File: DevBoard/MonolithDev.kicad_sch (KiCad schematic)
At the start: 4 parts

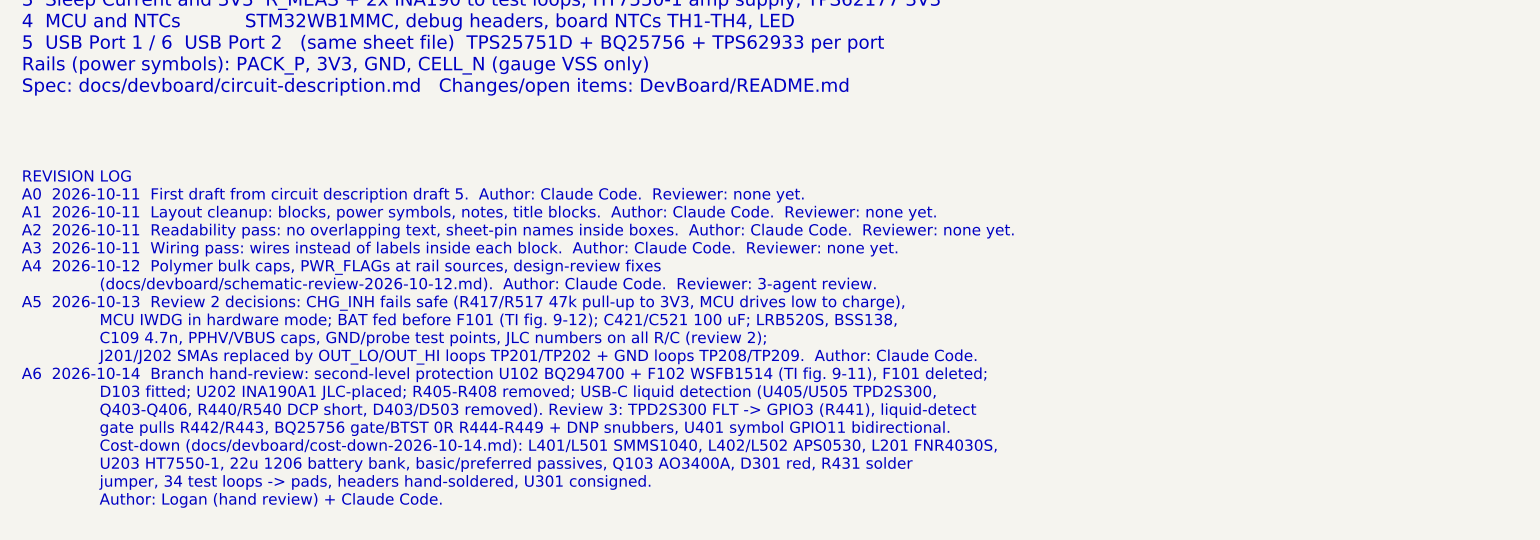
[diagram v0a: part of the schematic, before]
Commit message: Dev board: charger half-bridges -> discrete PGQ04N070 FETs
Each IAUC45N04S6L063H half-bridge ($1.16, 62 at JLC) becomes two JinYu
PGQ04N070 (C49384056, $0.12, PDFN3333 on the AGM PDFN3.3x3.3 footprint):
Q401/Q407 USB side, Q402/Q408 battery side, and the 5xx twins. 40 V,
10 mOhm max at 4.5 V (IAUC45: 8.5), Qg 14.7 nC; matches the production
plan of discrete 3.3 x 3.3 mm FETs. New PGQ04N070 symbol, power stage
redrawn, docs and costed BOM updated: about $77 per board at 5 boards.

Co-Authored-By: Claude Opus 5.5 <noreply@anthropic.com>
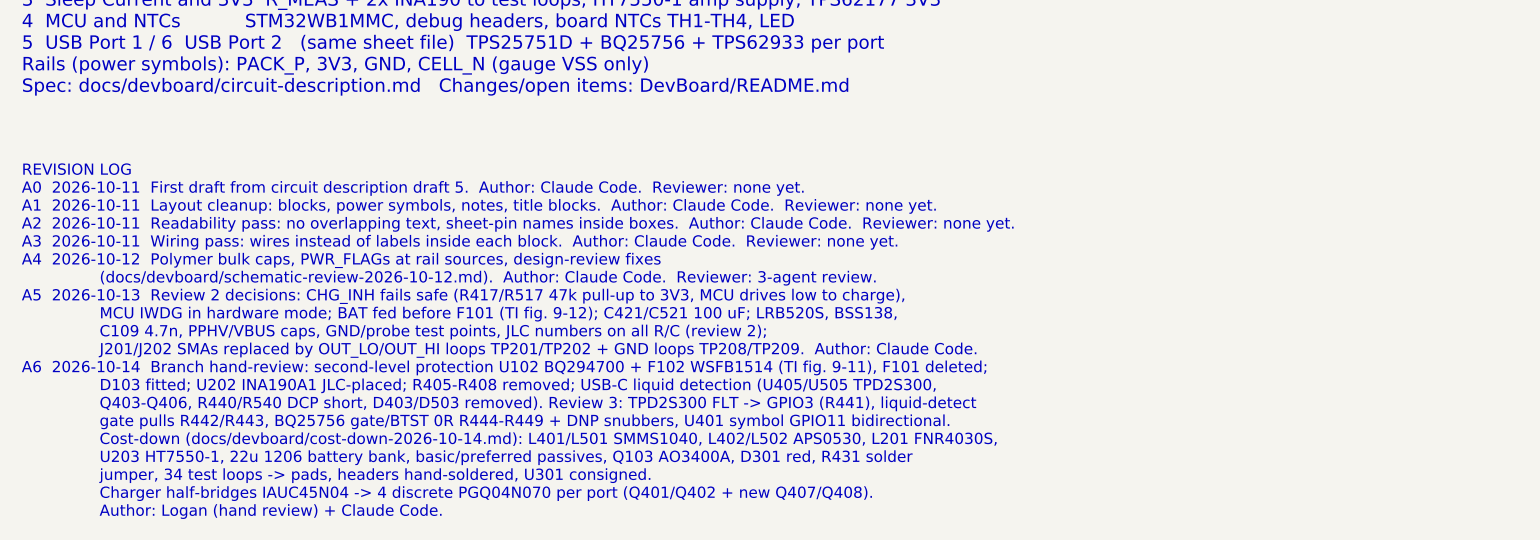
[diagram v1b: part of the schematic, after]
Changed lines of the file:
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@@
 		)
 	)
-	(text "REVISION LOG\nA0  2026-10-11  First draft from circuit description draft 5.  Author: Claude Code.  Reviewer: none yet.\nA1  2026-10-11  Layout cleanup: blocks, power symbols, notes, title blocks.  Author: Claude Code.  Reviewer: none yet.\nA2  2026-10-11  Readability pass: no overlapping text, sheet-pin names inside boxes.  Author: Claude Code.  Reviewer: none yet.\nA3  2026-10-11  Wiring pass: wires instead of labels inside each block.  Author: Claude Code.  Reviewer: none yet.\nA4  2026-10-12  Polymer bulk caps, PWR_FLAGs at rail sources, design-review fixes\n                (docs/devboard/schematic-review-2026-10-12.md).  Author: Claude Code.  Reviewer: 3-agent review.\nA5  2026-10-13  Review 2 decisions: CHG_INH fails safe (R417/R517 47k pull-up to 3V3, MCU drives low to charge),\n                MCU IWDG in hardware mode; BAT fed before F101 (TI fig. 9-12); C421/C521 100 uF; LRB520S, BSS138,\n                C109 4.7n, PPHV/VBUS caps, GND/probe test points, JLC numbers on all R/C (review 2);\n                J201/J202 SMAs replaced by OUT_LO/OUT_HI loops TP201/TP202 + GND loops TP208/TP209.  Author: Claude Code.\nA6  2026-10-14  Branch hand-review: second-level protection U102 BQ294700 + F102 WSFB1514 (TI fig. 9-11), F101 deleted;\n                D103 fitted; U202 INA190A1 JLC-placed; R405-R408 removed; USB-C liquid detection (U405/U505 TPD2S300,\n                Q403-Q406, R440/R540 DCP short, D403/D503 removed). Review 3: TPD2S300 FLT -> GPIO3 (R441), liquid-detect\n                gate pulls R442/R443, BQ25756 gate/BTST 0R R444-R449 + DNP snubbers, U401 symbol GPIO11 bidirectional.\n                Cost-down (docs/devboard/cost-down-2026-10-14.md): L401/L501 SMMS1040, L402/L502 APS0530, L201 FNR4030S,\n                U203 HT7550-1, 22u 1206 battery bank, basic/preferred passives, Q103 AO3400A, D301 red, R431 solder\n                jumper, 34 test loops -> pads, headers hand-soldered, U301 consigned.\n                Author: Logan (hand review) + Claude Code."
+	(text "REVISION LOG\nA0  2026-10-11  First draft from circuit description draft 5.  Author: Claude Code.  Reviewer: none yet.\nA1  2026-10-11  Layout cleanup: blocks, power symbols, notes, title blocks.  Author: Claude Code.  Reviewer: none yet.\nA2  2026-10-11  Readability pass: no overlapping text, sheet-pin names inside boxes.  Author: Claude Code.  Reviewer: none yet.\nA3  2026-10-11  Wiring pass: wires instead of labels inside each block.  Author: Claude Code.  Reviewer: none yet.\nA4  2026-10-12  Polymer bulk caps, PWR_FLAGs at rail sources, design-review fixes\n                (docs/devboard/schematic-review-2026-10-12.md).  Author: Claude Code.  Reviewer: 3-agent review.\nA5  2026-10-13  Review 2 decisions: CHG_INH fails safe (R417/R517 47k pull-up to 3V3, MCU drives low to charge),\n                MCU IWDG in hardware mode; BAT fed before F101 (TI fig. 9-12); C421/C521 100 uF; LRB520S, BSS138,\n                C109 4.7n, PPHV/VBUS caps, GND/probe test points, JLC numbers on all R/C (review 2);\n                J201/J202 SMAs replaced by OUT_LO/OUT_HI loops TP201/TP202 + GND loops TP208/TP209.  Author: Claude Code.\nA6  2026-10-14  Branch hand-review: second-level protection U102 BQ294700 + F102 WSFB1514 (TI fig. 9-11), F101 deleted;\n                D103 fitted; U202 INA190A1 JLC-placed; R405-R408 removed; USB-C liquid detection (U405/U505 TPD2S300,\n                Q403-Q406, R440/R540 DCP short, D403/D503 removed). Review 3: TPD2S300 FLT -> GPIO3 (R441), liquid-detect\n                gate pulls R442/R443, BQ25756 gate/BTST 0R R444-R449 + DNP snubbers, U401 symbol GPIO11 bidirectional.\n                Cost-down (docs/devboard/cost-down-2026-10-14.md): L401/L501 SMMS1040, L402/L502 APS0530, L201 FNR4030S,\n                U203 HT7550-1, 22u 1206 battery bank, basic/preferred passives, Q103 AO3400A, D301 red, R431 solder\n                jumper, 34 test loops -> pads, headers hand-soldered, U301 consigned.\n                Charger half-bridges IAUC45N04 -> 4 discrete PGQ04N070 per port (Q401/Q402 + new Q407/Q408).\n                Author: Logan (hand review) + Claude Code."
 		(exclude_from_sim no)
-		(at 30.48 252.73 0)
+		(at 30.48 254.0 0)
 		(effects
 			(font

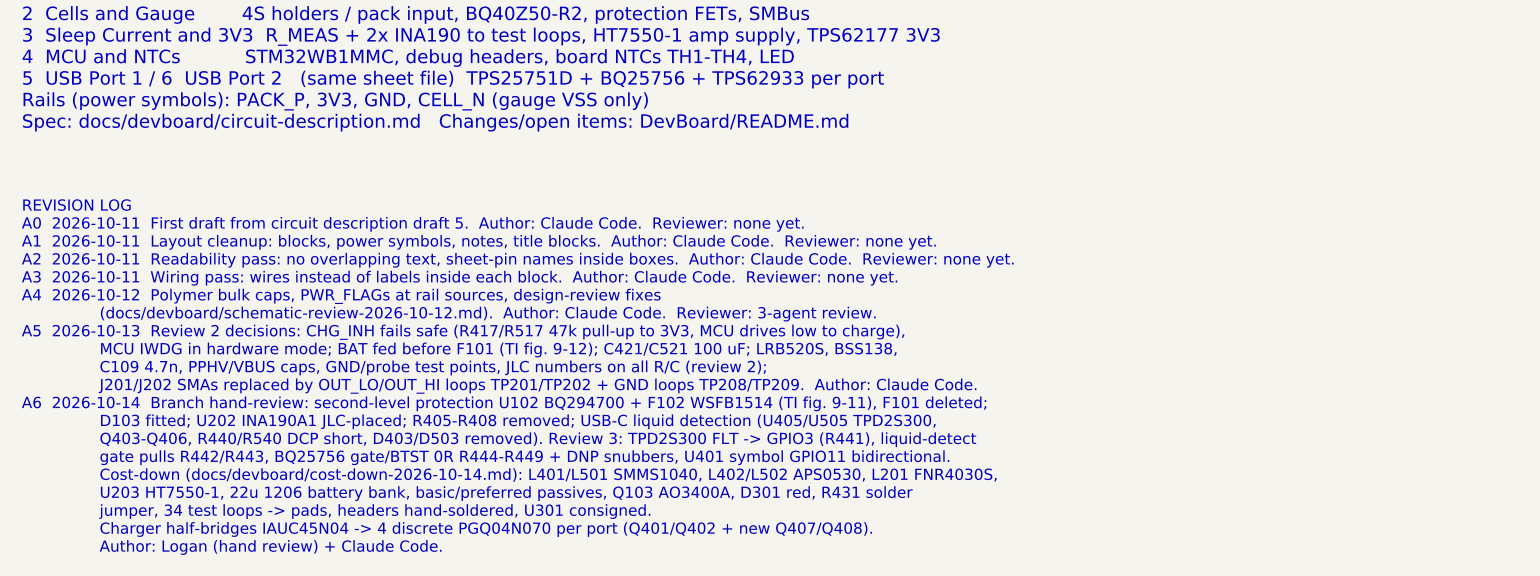
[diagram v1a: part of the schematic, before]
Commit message: Dev board: 6-layer 1.6 mm board, TPD4S201 port protector, 1.6 mm USB-C
- Stack-up: 6 layers, 1.6 mm, 2 oz outer / 0.5 oz inner (In1/In4 GND),
  0.3 mm drill / 0.45 mm via minimum so JLC's small-via surcharge is gone.
  Via-in-pad (POFV) is free on 6+ layers.
- U405/U505: TPD2S300 (0.4 mm DSBGA) -> TPD4S201TRGRRQ1 (VQFN-20 RGR),
  CC + SBU protection with FLT -> GPIO3. D402/D502 and C453/C553 removed.
- J401/J501: Shou Han TYPE-C 16PCB1.6 IP68 (C55629729), footprint and
  STEP model generated for the 1.6 mm board.
- TPS25751 REF0038A thermal vias 0.2 -> 0.3 mm.
- setup_board.py keeps unmanaged net classes (Kelvin); reset_board.py
  reloads swapped footprints in place.
- ERC 0 errors, DRC schematic parity 0. BOM $77.17 -> $78.65 per board
  at 5 boards.

Co-Authored-By: Claude Opus 5.5 <noreply@anthropic.com>
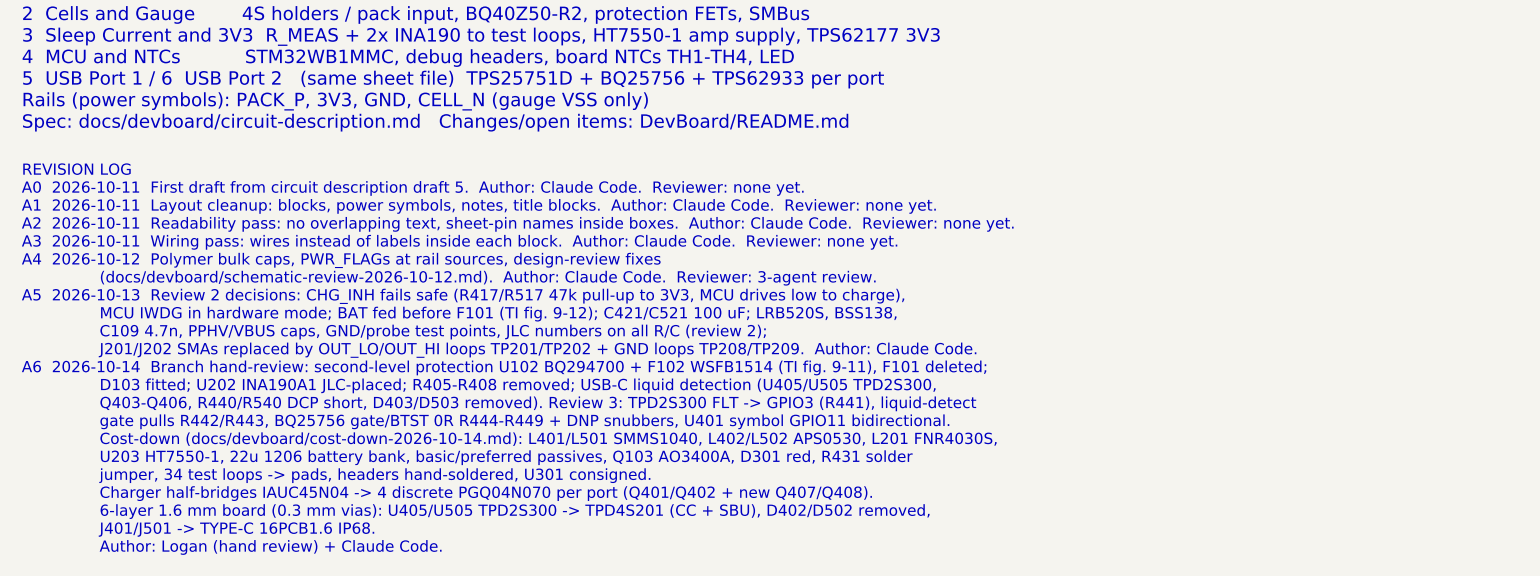
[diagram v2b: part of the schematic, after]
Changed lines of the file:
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@@
 		)
 	)
-	(text "REVISION LOG\nA0  2026-10-11  First draft from circuit description draft 5.  Author: Claude Code.  Reviewer: none yet.\nA1  2026-10-11  Layout cleanup: blocks, power symbols, notes, title blocks.  Author: Claude Code.  Reviewer: none yet.\nA2  2026-10-11  Readability pass: no overlapping text, sheet-pin names inside boxes.  Author: Claude Code.  Reviewer: none yet.\nA3  2026-10-11  Wiring pass: wires instead of labels inside each block.  Author: Claude Code.  Reviewer: none yet.\nA4  2026-10-12  Polymer bulk caps, PWR_FLAGs at rail sources, design-review fixes\n                (docs/devboard/schematic-review-2026-10-12.md).  Author: Claude Code.  Reviewer: 3-agent review.\nA5  2026-10-13  Review 2 decisions: CHG_INH fails safe (R417/R517 47k pull-up to 3V3, MCU drives low to charge),\n                MCU IWDG in hardware mode; BAT fed before F101 (TI fig. 9-12); C421/C521 100 uF; LRB520S, BSS138,\n                C109 4.7n, PPHV/VBUS caps, GND/probe test points, JLC numbers on all R/C (review 2);\n                J201/J202 SMAs replaced by OUT_LO/OUT_HI loops TP201/TP202 + GND loops TP208/TP209.  Author: Claude Code.\nA6  2026-10-14  Branch hand-review: second-level protection U102 BQ294700 + F102 WSFB1514 (TI fig. 9-11), F101 deleted;\n                D103 fitted; U202 INA190A1 JLC-placed; R405-R408 removed; USB-C liquid detection (U405/U505 TPD2S300,\n                Q403-Q406, R440/R540 DCP short, D403/D503 removed). Review 3: TPD2S300 FLT -> GPIO3 (R441), liquid-detect\n                gate pulls R442/R443, BQ25756 gate/BTST 0R R444-R449 + DNP snubbers, U401 symbol GPIO11 bidirectional.\n                Cost-down (docs/devboard/cost-down-2026-10-14.md): L401/L501 SMMS1040, L402/L502 APS0530, L201 FNR4030S,\n                U203 HT7550-1, 22u 1206 battery bank, basic/preferred passives, Q103 AO3400A, D301 red, R431 solder\n                jumper, 34 test loops -> pads, headers hand-soldered, U301 consigned.\n                Charger half-bridges IAUC45N04 -> 4 discrete PGQ04N070 per port (Q401/Q402 + new Q407/Q408).\n                Author: Logan (hand review) + Claude Code."
+	(text "REVISION LOG\nA0  2026-10-11  First draft from circuit description draft 5.  Author: Claude Code.  Reviewer: none yet.\nA1  2026-10-11  Layout cleanup: blocks, power symbols, notes, title blocks.  Author: Claude Code.  Reviewer: none yet.\nA2  2026-10-11  Readability pass: no overlapping text, sheet-pin names inside boxes.  Author: Claude Code.  Reviewer: none yet.\nA3  2026-10-11  Wiring pass: wires instead of labels inside each block.  Author: Claude Code.  Reviewer: none yet.\nA4  2026-10-12  Polymer bulk caps, PWR_FLAGs at rail sources, design-review fixes\n                (docs/devboard/schematic-review-2026-10-12.md).  Author: Claude Code.  Reviewer: 3-agent review.\nA5  2026-10-13  Review 2 decisions: CHG_INH fails safe (R417/R517 47k pull-up to 3V3, MCU drives low to charge),\n                MCU IWDG in hardware mode; BAT fed before F101 (TI fig. 9-12); C421/C521 100 uF; LRB520S, BSS138,\n                C109 4.7n, PPHV/VBUS caps, GND/probe test points, JLC numbers on all R/C (review 2);\n                J201/J202 SMAs replaced by OUT_LO/OUT_HI loops TP201/TP202 + GND loops TP208/TP209.  Author: Claude Code.\nA6  2026-10-14  Branch hand-review: second-level protection U102 BQ294700 + F102 WSFB1514 (TI fig. 9-11), F101 deleted;\n                D103 fitted; U202 INA190A1 JLC-placed; R405-R408 removed; USB-C liquid detection (U405/U505 TPD2S300,\n                Q403-Q406, R440/R540 DCP short, D403/D503 removed). Review 3: TPD2S300 FLT -> GPIO3 (R441), liquid-detect\n                gate pulls R442/R443, BQ25756 gate/BTST 0R R444-R449 + DNP snubbers, U401 symbol GPIO11 bidirectional.\n                Cost-down (docs/devboard/cost-down-2026-10-14.md): L401/L501 SMMS1040, L402/L502 APS0530, L201 FNR4030S,\n                U203 HT7550-1, 22u 1206 battery bank, basic/preferred passives, Q103 AO3400A, D301 red, R431 solder\n                jumper, 34 test loops -> pads, headers hand-soldered, U301 consigned.\n                Charger half-bridges IAUC45N04 -> 4 discrete PGQ04N070 per port (Q401/Q402 + new Q407/Q408).\n                6-layer 1.6 mm board (0.3 mm vias): U405/U505 TPD2S300 -> TPD4S201 (CC + SBU), D402/D502 removed,\n                J401/J501 -> TYPE-C 16PCB1.6 IP68.\n                Author: Logan (hand review) + Claude Code."
 		(exclude_from_sim no)
 		(at 30.48 254.0 0)
